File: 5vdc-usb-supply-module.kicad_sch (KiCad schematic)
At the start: 0 parts

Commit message: Draft 5VDC Supply Schematic
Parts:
- added F4: Fuse, symbol Device:Fuse
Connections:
- new net 5VDC_SUPPLY: F4.1
- new net 5VDC_USB_FUSED_SUPPLY: F4.2
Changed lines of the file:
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@@
     (company "eatmellc")
   )
+  (global_label "5VDC_SUPPLY" (shape input) (at 59.69 68.58 180) (fields_autoplaced)
+    (effects (font (size 1.27 1.27)) (justify right))
+    (property "Intersheet References" "${INTERSHEET_REFS}" (id 0) (at 44.2745 68.5006 0)
+      (effects (font (size 1.27 1.27)) (justify right))
+    )
+  )
+  (global_label "5VDC_USB_FUSED_SUPPLY" (shape input) (at 67.31 68.58 0) (fields_autoplaced)
+    (effects (font (size 1.27 1.27)) (justify left))
+    (property "Intersheet References" "${INTERSHEET_REFS}" (id 0) (at 94.5183 68.5006 0)
+      (effects (font (size 1.27 1.27)) (justify left))
+    )
+  )
+  (symbol (lib_id "Device:Fuse") (at 63.5 68.58 90) (unit 1)
+    (in_bom yes) (on_board yes) (fields_autoplaced)
+    (property "Reference" "F4" (id 0) (at 63.5 62.23 90))
+    (property "Value" "Fuse" (id 1) (at 63.5 64.77 90))
+    (property "Footprint" "" (id 2) (at 63.5 70.358 90)
+      (effects (font (size 1.27 1.27)) hide)
+    )
+    (property "Datasheet" "~" (id 3) (at 63.5 68.58 0)
+      (effects (font (size 1.27 1.27)) hide)
+    )
+    (pin "1")
+    (pin "2")
+  )
 )

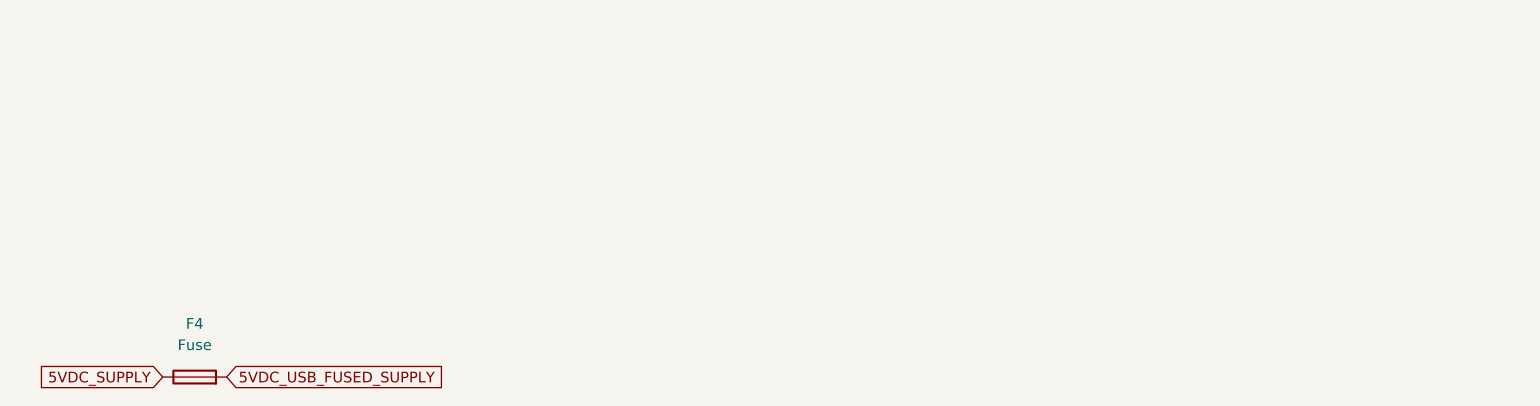
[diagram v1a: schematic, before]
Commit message: Save more changes
Started Fan Control
Created VDC Meter Template
Fleshed out 12, 5, 5-usb, and 3.3 modules
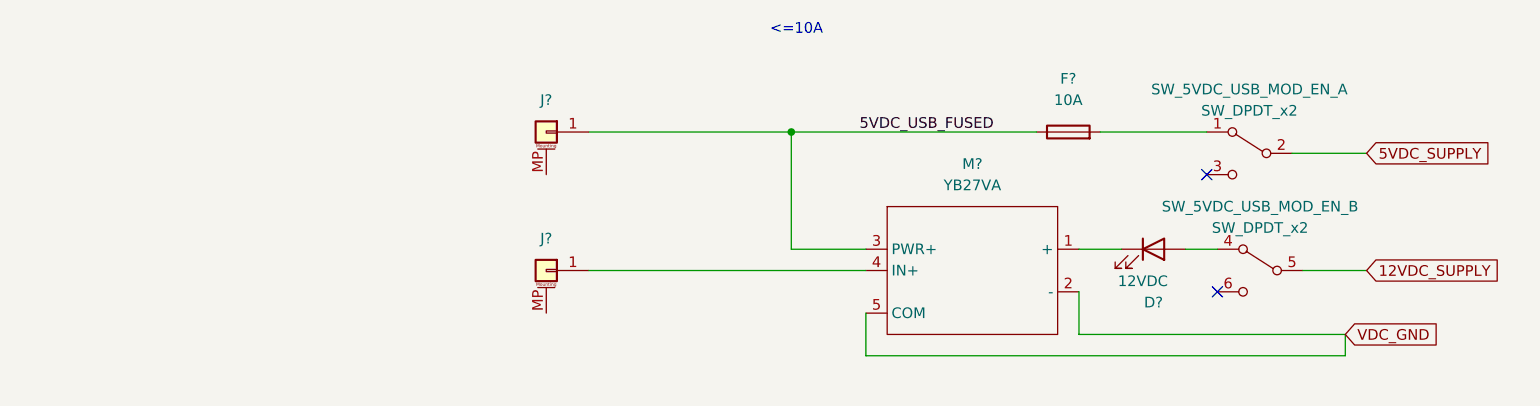
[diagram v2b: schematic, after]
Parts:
- removed F4: Fuse, symbol Device:Fuse
- added D?: 12VDC, symbol Device:LED
- added F?: 10A, symbol Device:Fuse
- added J? (x2): Conn_01x01_MountingPin, symbol Connector_Generic_MountingPin:Conn_01x01_MountingPin
- added M?: YB27VA, symbol bvm-library:5_Pin_Meter_With_Ext_Shunt
- added SW_5VDC_USB_MOD_EN_: SW_DPDT_x2, symbol Switch:SW_DPDT_x2
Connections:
- net 5VDC_SUPPLY: now also SW_5VDC_USB_MOD_EN_.2 (B)
- new net: J?.1 (Pin_1), M?.4 (IN+)
- new net: D?.1 (K), M?.1 (+)
- new net: F?.2, SW_5VDC_USB_MOD_EN_.1 (A)
- new net: D?.2 (A), SW_5VDC_USB_MOD_EN_.4 (A)
- new net 12VDC_SUPPLY: SW_5VDC_USB_MOD_EN_.5 (B)
- new net 5VDC_USB_FUSED: F?.1, J?.1 (Pin_1), M?.3 (PWR+)
- new net VDC_GND: M?.2 (-), M?.5 (COM)
- no-connect marks 0 -> 2
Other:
- note added: "<=10A"

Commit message: Bunch more changes
Blah blah
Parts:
- removed J? (x2): Conn_01x01_MountingPin, symbol Connector_Generic_MountingPin:Conn_01x01_MountingPin
- added F?: 10A, symbol Device:Fuse
- added M?: YB27VA, symbol bvm-library:5_Pin_Meter_With_Ext_Shunt
- added SW_5VDC_USB_MOD_EN: SW_SPST_LED_3pin, symbol bvm-library:SW_SPST_LED_3pin
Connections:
- net 12VDC_SUPPLY: now also M?.1 (+)
- net 5VDC_USB_FUSED: now also F?.1, M?.3 (PWR+)
- net VDC_GND: now also M?.2 (-), M?.5 (COM), SW_5VDC_USB_MOD_EN.4 (A)
- net GND: now reaches M?.4 (IN+)
- net GND: now also M?.4 (IN+)
- new net: F?.2, SW_5VDC_USB_MOD_EN.1
- no-connect marks 2 -> 3
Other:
- note added: "[5VDC USB MODULE ACTIVE]"
- title: (none) -> Mr. Powers
- moved on the sheet: F?

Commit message: Minor change across the board
I need better notes.
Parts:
- gave numbers to parts that had none: 5
- renumbered SW_5VDC_USB_MOD_EN to SW_5VDC_USB_MOD_EN1, SW_5VDC_USB_MOD_EN_ to SW_5VDC_USB_MOD_EN_1
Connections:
- net 5VDC_SUPPLY: now also SW_5VDC_USB_MOD_EN1.2
- net VDC_GND: now also SW_5VDC_USB_MOD_EN1.3 (A); no longer SW_5VDC_USB_MOD_EN1.4 (A)
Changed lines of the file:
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@@
     (stroke (width 0) (type default) (color 255 255 0 1))
+  )
+  (wire (pts (xy 205.74 109.22) (xy 213.36 109.22))
+    (stroke (width 0) (type default) (color 0 0 0 0))
   )
   (wire (pts (xy 180.34 123.19) (xy 185.42 123.19))
@@
   (symbol (lib_id "Device:Fuse") (at 167.64 109.22 90) (unit 1)
     (in_bom yes) (on_board yes) (fields_autoplaced)
-    (property "Reference" "F?" (id 0) (at 167.64 102.87 90))
+    (property "Reference" "F5" (id 0) (at 167.64 102.87 90))
     (property "Value" "10A" (id 1) (at 167.64 105.41 90))
     (property "Footprint" "" (id 2) (at 167.64 110.998 90)
@@
   (symbol (lib_id "bvm-library:5_Pin_Meter_With_Ext_Shunt") (at 162.56 128.27 0) (unit 1)
     (in_bom yes) (on_board yes) (fields_autoplaced)
-    (property "Reference" "M?" (id 0) (at 167.64 113.03 0))
+    (property "Reference" "M8" (id 0) (at 167.64 113.03 0))
     (property "Value" "YB27VA" (id 1) (at 167.64 115.57 0))
     (property "Footprint" "" (id 2) (at 162.56 128.27 0)
@@
   (symbol (lib_id "bvm-library:SW_SPST_LED_3pin") (at 200.66 111.76 0) (unit 1)
     (in_bom yes) (on_board yes) (fields_autoplaced)
-    (property "Reference" "SW_5VDC_USB_MOD_EN" (id 0) (at 200.025 102.87 0))
+    (property "Reference" "SW_5VDC_USB_MOD_EN1" (id 0) (at 200.025 102.87 0))
     (property "Value" "SW_SPST_LED_3pin" (id 1) (at 200.025 105.41 0))
     (property "Footprint" "" (id 2) (at 200.66 104.14 0)
@@
     (pin "1")
     (pin "2")
-    (pin "4")
+    (pin "3")
   )
   (symbol (lib_id "bvm-library:USB_PWR_A") (at 92.71 53.34 0) (unit 1)
     (in_bom no) (on_board no) (fields_autoplaced)
-    (property "Reference" "J?" (id 0) (at 92.71 40.64 0))
+    (property "Reference" "#J012" (id 0) (at 92.71 40.64 0))
     (property "Value" "USB_PWR_A" (id 1) (at 92.71 43.18 0))
     (property "Footprint" "" (id 2) (at 96.52 54.61 0)
@@
   (symbol (lib_id "bvm-library:5_Pin_Meter_With_Ext_Shunt") (at 151.13 58.42 0) (unit 1)
     (in_bom yes) (on_board yes) (fields_autoplaced)
-    (property "Reference" "M?" (id 0) (at 156.21 43.18 0))
+    (property "Reference" "M7" (id 0) (at 156.21 43.18 0))
     (property "Value" "YB27VA" (id 1) (at 156.21 45.72 0))
     (property "Footprint" "" (id 2) (at 151.13 58.42 0)
@@
   (symbol (lib_id "Device:Fuse") (at 156.21 39.37 90) (unit 1)
     (in_bom yes) (on_board yes) (fields_autoplaced)
-    (property "Reference" "F?" (id 0) (at 156.21 33.02 90))
+    (property "Reference" "F4" (id 0) (at 156.21 33.02 90))
     (property "Value" "10A" (id 1) (at 156.21 35.56 90))
     (property "Footprint" "" (id 2) (at 156.21 41.148 90)
@@
   (symbol (lib_id "Switch:SW_DPDT_x2") (at 189.23 41.91 0) (mirror y) (unit 1)
     (in_bom yes) (on_board yes) (fields_autoplaced)
-    (property "Reference" "SW_5VDC_USB_MOD_EN_" (id 0) (at 189.23 34.29 0))
+    (property "Reference" "SW_5VDC_USB_MOD_EN_1" (id 0) (at 189.23 34.29 0))
     (property "Value" "SW_DPDT_x2" (id 1) (at 189.23 36.83 0))
     (property "Footprint" "" (id 2) (at 189.23 41.91 0)
@@
   (symbol (lib_id "bvm-library:USB_PWR_A") (at 104.14 123.19 0) (unit 1)
     (in_bom no) (on_board no) (fields_autoplaced)
-    (property "Reference" "J?" (id 0) (at 104.14 110.49 0))
+    (property "Reference" "#J013" (id 0) (at 104.14 110.49 0))
     (property "Value" "USB_PWR_A" (id 1) (at 104.14 113.03 0))
     (property "Footprint" "" (id 2) (at 107.95 124.46 0)
@@
   (symbol (lib_id "Device:LED") (at 177.8 53.34 0) (unit 1)
     (in_bom yes) (on_board yes)
-    (property "Reference" "D?" (id 0) (at 177.8 59.69 0))
+    (property "Reference" "D5" (id 0) (at 177.8 59.69 0))
     (property "Value" "12VDC" (id 1) (at 176.53 57.15 0))
     (property "Footprint" "" (id 2) (at 177.8 53.34 0)
@@
   (symbol (lib_id "Switch:SW_DPDT_x2") (at 190.5 55.88 0) (mirror y) (unit 2)
     (in_bom yes) (on_board yes) (fields_autoplaced)
-    (property "Reference" "SW_5VDC_USB_MOD_EN_" (id 0) (at 190.5 48.26 0))
+    (property "Reference" "SW_5VDC_USB_MOD_EN_1" (id 0) (at 190.5 48.26 0))
     (property "Value" "SW_DPDT_x2" (id 1) (at 190.5 50.8 0))
     (property "Footprint" "" (id 2) (at 190.5 55.88 0)
